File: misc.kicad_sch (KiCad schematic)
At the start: 36 parts

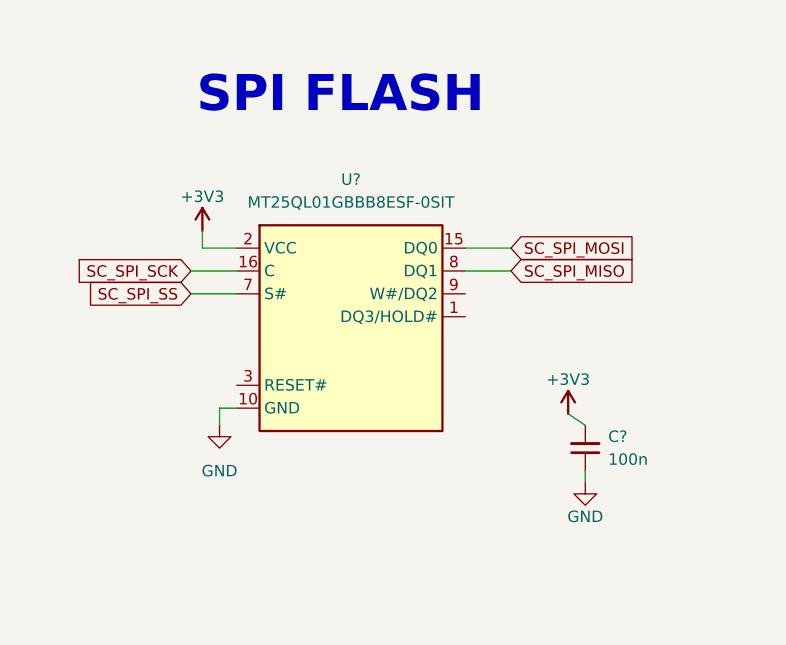
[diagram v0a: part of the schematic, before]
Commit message: [#54272] Change MT25QL01GBBB package
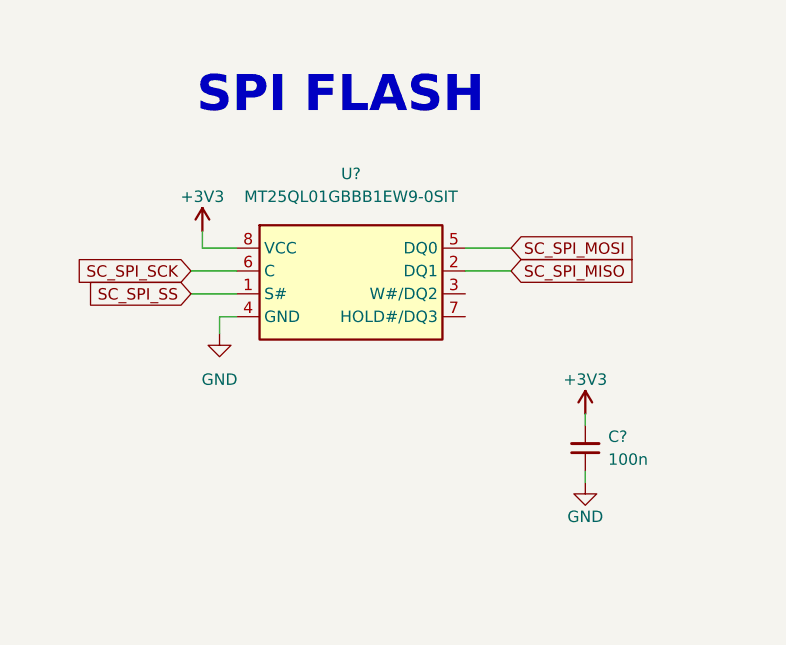
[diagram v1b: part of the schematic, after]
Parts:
- removed U?: MT25QL01GBBB8E_SOP2-16, antmicro-footprints:SOP2-16_7.5x10.3mm, symbol antmicroMemory:MT25QL01GBBB8E_SOP2-16
- added U?: MT25QL01GBBB1EW9-0SIT, antmicro-footprints:W-PDFN-8-1EP_8x6mm_P1.27mm_EP4.3x3.4mm, symbol antmicroMemory:MT25QL01GBBB1EW9-0SIT
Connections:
- net +3V3: now also U?.8 (VCC)
- net GND: now also U?.4 (GND)
- net SC_SPI_MISO: now also U?.2 (DQ1)
- net SC_SPI_MOSI: now also U?.5 (DQ0)
- net SC_SPI_SCK: now also U?.6 (C)
- net SC_SPI_SS: now also U?.1 (S#)
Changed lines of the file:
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@@
     (stroke (width 0) (type default) (color 0 0 0 0))
   )
-  (wire (pts (xy 385.445 204.47) (xy 387.35 205.74))
+  (wire (pts (xy 387.35 204.47) (xy 387.35 205.74))
     (stroke (width 0) (type default) (color 0 0 0 0))
   )
@@
     (stroke (width 0) (type default) (color 0 0 0 0))
   )
-  (wire (pts (xy 348.615 203.835) (xy 346.71 203.835))
+  (wire (pts (xy 348.615 193.675) (xy 346.71 193.675))
     (stroke (width 0) (type default) (color 0 0 0 0))
   )
@@
     (stroke (width 0) (type default) (color 0 0 0 0))
   )
-  (wire (pts (xy 346.71 203.835) (xy 346.71 205.74))
+  (wire (pts (xy 346.71 193.675) (xy 346.71 195.58))
     (stroke (width 0) (type default) (color 0 0 0 0))
   )
@@
     )
   )
-  (symbol (lib_id "antmicropower:+3V3") (at 385.445 204.47 0) (unit 1)
+  (symbol (lib_id "antmicropower:+3V3") (at 387.35 204.47 0) (unit 1)
     (in_bom yes) (on_board yes)
-    (property "Reference" "#PWR?" (id 0) (at 400.685 207.01 0)
+    (property "Reference" "#PWR?" (id 0) (at 402.59 207.01 0)
       (effects (font (size 1.27 1.27) (thickness 0.15)) (justify left bottom) hide)
     )
-    (property "Value" "+3V3" (id 1) (at 385.445 200.66 0)
+    (property "Value" "+3V3" (id 1) (at 387.35 200.66 0)
       (effects (font (size 1.27 1.27) (thickness 0.15)))
     )
-    (property "Footprint" "" (id 2) (at 400.685 212.09 0)
+    (property "Footprint" "" (id 2) (at 402.59 212.09 0)
       (effects (font (size 1.27 1.27) (thickness 0.15)) (justify left bottom) hide)
     )
-    (property "Datasheet" "" (id 3) (at 400.685 214.63 0)
+    (property "Datasheet" "" (id 3) (at 402.59 214.63 0)
       (effects (font (size 1.27 1.27) (thickness 0.15)) (justify left bottom) hide)
     )
-    (property "Author" "Antmicro" (id 4) (at 400.685 212.09 0)
+    (property "Author" "Antmicro" (id 4) (at 402.59 212.09 0)
       (effects (font (size 1.27 1.27) (thickness 0.15)) (justify left bottom) hide)
     )
-    (property "License" "Apache-2.0" (id 5) (at 400.685 214.63 0)
+    (property "License" "Apache-2.0" (id 5) (at 402.59 214.63 0)
       (effects (font (size 1.27 1.27) (thickness 0.15)) (justify left bottom) hide)
     )
@@
     (pin "1")
   )
-  (symbol (lib_id "antmicropower:GND") (at 346.71 205.74 0) (unit 1)
+  (symbol (lib_id "antmicropower:GND") (at 346.71 195.58 0) (unit 1)
     (in_bom yes) (on_board yes) (fields_autoplaced)
-    (property "Reference" "#PWR?" (id 0) (at 355.6 208.28 0)
+    (property "Reference" "#PWR?" (id 0) (at 355.6 198.12 0)
       (effects (font (size 1.27 1.27) (thickness 0.15)) (justify left bottom) hide)
     )
-    (property "Value" "GND" (id 1) (at 346.71 210.82 0)
+    (property "Value" "GND" (id 1) (at 346.71 200.66 0)
       (effects (font (size 1.27 1.27) (thickness 0.15)))
     )
-    (property "Footprint" "" (id 2) (at 355.6 213.36 0)
+    (property "Footprint" "" (id 2) (at 355.6 203.2 0)
       (effects (font (size 1.27 1.27) (thickness 0.15)) (justify left bottom) hide)
     )
-    (property "Datasheet" "" (id 3) (at 355.6 218.44 0)
+    (property "Datasheet" "" (id 3) (at 355.6 208.28 0)
       (effects (font (size 1.27 1.27) (thickness 0.15)) (justify left bottom) hide)
     )
-    (property "Author" "Antmicro" (id 4) (at 355.6 213.36 0)
+    (property "Author" "Antmicro" (id 4) (at 355.6 203.2 0)
       (effects (font (size 1.27 1.27) (thickness 0.15)) (justify left bottom) hide)
     )
-    (property "License" "Apache-2.0" (id 5) (at 355.6 215.9 0)
+    (property "License" "Apache-2.0" (id 5) (at 355.6 205.74 0)
       (effects (font (size 1.27 1.27) (thickness 0.15)) (justify left bottom) hide)
     )
     (pin "1")
   )
-  (symbol (lib_id "antmicroMemory:MT25QL01GBBB8E_SOP2-16") (at 346.075 186.055 0) (unit 1)
-    (in_bom yes) (on_board yes) (fields_autoplaced)
-    (property "Reference" "U?" (id 0) (at 361.315 178.435 0)
-      (effects (font (size 1.27 1.27) (thickness 0.15)))
-    )
-    (property "Value" "MT25QL01GBBB8E_SOP2-16" (id 1) (at 389.255 193.675 0)
-      (effects (font (size 1.27 1.27) (thickness 0.15)) (justify left bottom) hide)
-    )
-    (property "Footprint" "antmicro-footprints:SOP2-16_7.5x10.3mm" (id 2) (at 389.255 196.215 0)
-      (effects (font (size 1.27 1.27) (thickness 0.15)) (justify left bottom) hide)
-    )
-    (property "Datasheet" "https://www.mouser.com/datasheet/2/671/mict_s_a0005338280_1-2290790.pdf" (id 3) (at 389.255 198.755 0)
-      (effects (font (size 1.27 1.27) (thickness 0.15)) (justify left bottom) hide)
-    )
-    (property "MPN" "MT25QL01GBBB8ESF-0SIT" (id 4) (at 361.315 180.975 0)
-      (effects (font (size 1.27 1.27) (thickness 0.15)))
-    )
-    (property "Manufacturer" "Micron Technology" (id 5) (at 389.255 201.295 0)
-      (effects (font (size 1.27 1.27) (thickness 0.15)) (justify left bottom) hide)
-    )
-    (property "VSD_class" "SPI Flash" (id 6) (at 389.255 203.835 0)
-      (effects (font (size 1.27 1.27) (thickness 0.15)) (justify left bottom) hide)
-    )
-    (property "Author" "Antmicro" (id 7) (at 389.255 206.375 0)
-      (effects (font (size 1.27 1.27) (thickness 0.15)) (justify left bottom) hide)
-    )
-    (property "License" "Apache-2.0" (id 8) (at 389.255 208.915 0)
-      (effects (font (size 1.27 1.27) (thickness 0.15)) (justify left bottom) hide)
-    )
-    (pin "1")
-    (pin "10")
-    (pin "11")
-    (pin "12")
-    (pin "13")
-    (pin "14")
-    (pin "15")
-    (pin "16")
-    (pin "2")
-    (pin "3")
-    (pin "4")
-    (pin "5")
-    (pin "6")
-    (pin "7")
-    (pin "8")
-    (pin "9")
-  )
   (symbol (lib_id "antmicroResistors0402:R_49k9_0402") (at 264.16 181.61 90) (unit 1)
     (in_bom yes) (on_board yes)
@@
     (pin "2")
   )
+  (symbol (lib_id "antmicroMemory:MT25QL01GBBB1EW9-0SIT ") (at 348.615 186.055 0) (unit 1)
+    (in_bom yes) (on_board yes) (fields_autoplaced)
+    (property "Reference" "U?" (id 0) (at 361.315 177.8 0)
+      (effects (font (size 1.27 1.27) (thickness 0.15)))
+    )
+    (property "Value" "MT25QL01GBBB1EW9-0SIT " (id 1) (at 391.795 193.675 0)
+      (effects (font (size 1.27 1.27) (thickness 0.15)) (justify left bottom) hide)
+    )
+    (property "Footprint" "antmicro-footprints:W-PDFN-8-1EP_8x6mm_P1.27mm_EP4.3x3.4mm" (id 2) (at 391.795 196.215 0)
+      (effects (font (size 1.27 1.27) (thickness 0.15)) (justify left bottom) hide)
+    )
+    (property "Datasheet" "https://www.mouser.pl/datasheet/2/671/mict_s_a0002234966_1-2290738.pdf" (id 3) (at 391.795 198.755 0)
+      (effects (font (size 1.27 1.27) (thickness 0.15)) (justify left bottom) hide)
+    )
+    (property "MPN" "MT25QL01GBBB1EW9-0SIT " (id 4) (at 361.315 180.34 0)
+      (effects (font (size 1.27 1.27) (thickness 0.15)))
+    )
+    (property "Manufacturer" "Micron Technology" (id 5) (at 391.795 201.295 0)
+      (effects (font (size 1.27 1.27) (thickness 0.15)) (justify left bottom) hide)
+    )
+    (property "VSD_class" "SPI Flash" (id 6) (at 391.795 203.835 0)
+      (effects (font (size 1.27 1.27) (thickness 0.15)) (justify left bottom) hide)
+    )
+    (property "Author" "Antmicro" (id 7) (at 391.795 206.375 0)
+      (effects (font (size 1.27 1.27) (thickness 0.15)) (justify left bottom) hide)
+    )
+    (property "License" "Apache-2.0" (id 8) (at 391.795 208.915 0)
+      (effects (font (size 1.27 1.27) (thickness 0.15)) (justify left bottom) hide)
+    )
+    (pin "1")
+    (pin "2")
+    (pin "3")
+    (pin "4")
+    (pin "5")
+    (pin "6")
+    (pin "7")
+    (pin "8")
+  )
   (symbol (lib_id "antmicroResistors0402:R_49k9_0402") (at 261.62 181.61 90) (unit 1)

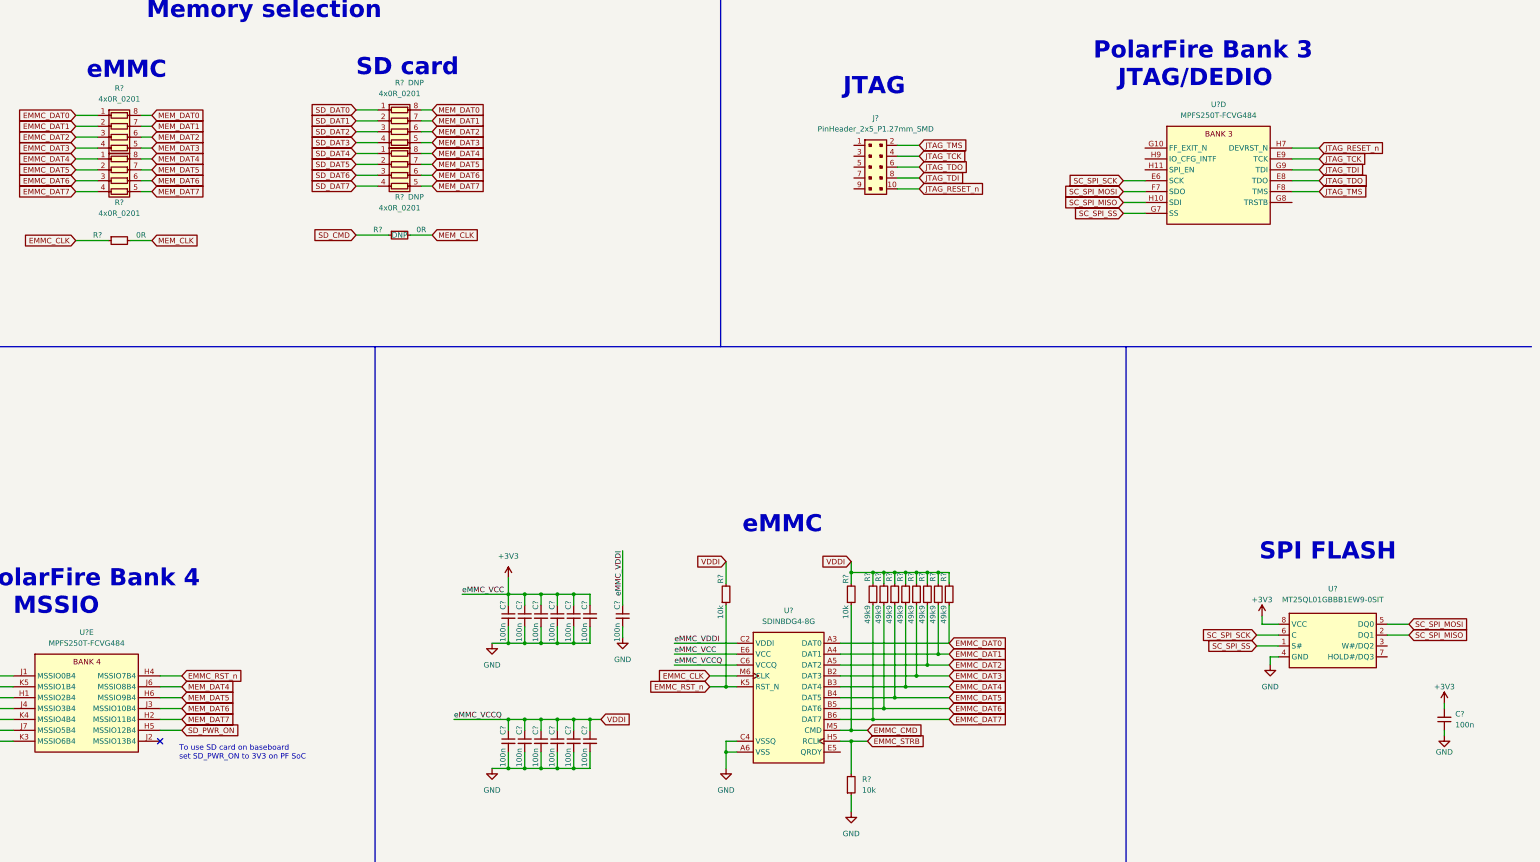
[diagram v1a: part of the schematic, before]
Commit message: [#54016] Place components to assess available space
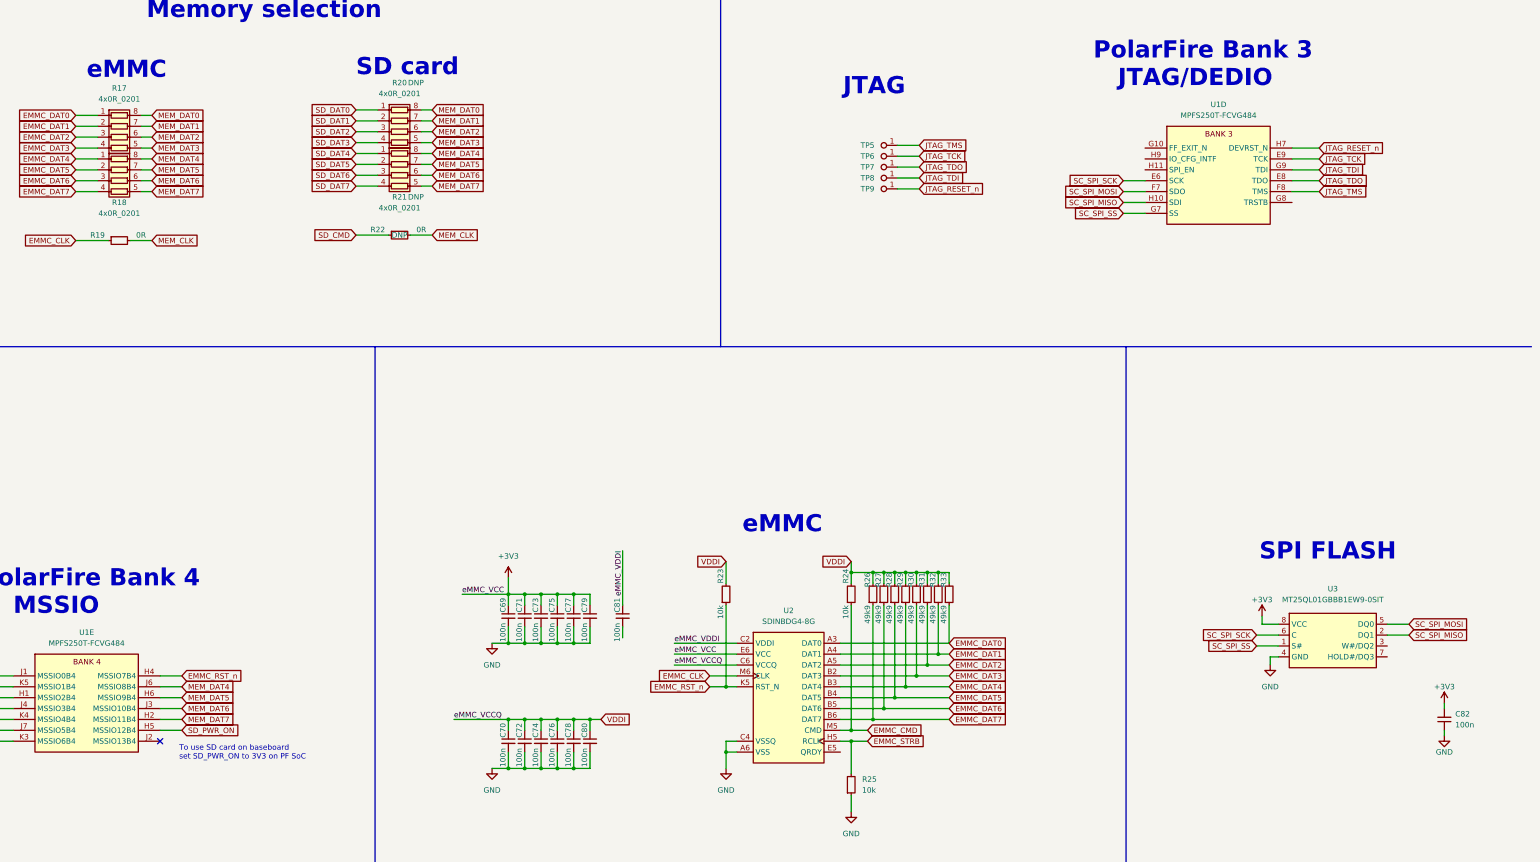
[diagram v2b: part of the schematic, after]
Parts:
- removed J?: PinHeader_2x5_P1.27mm_SMD, antmicro-footprints:PinHeader_2x5_P1.27mm_SMD, symbol antmicroGenericPinHeaders:PinHeader_2x5_P1.27mm_SMD
- removed U?: MT25QL01GBBB1EW9-0SIT, antmicro-footprints:W-PDFN-8-1EP_8x6mm_P1.27mm_EP4.3x3.4mm, symbol antmicroMemory:MT25QL01GBBB1EW9-0SIT
- added TP5, TP6, TP7, TP8, TP9: TP_0.75mm_SMD, antmicro-footprints:TP_SMD_0.75mm, symbol antmicroTestPoints:TP_0.75mm_SMD
- added U3: MT25QL01GBBB1EW9-0SIT, antmicro-footprints:W-PDFN-8-1EP_8x6mm_P1.27mm_EP4.3x3.4mm, symbol antmicroMemory:MT25QL01GBBB1EW9-0SIT
- gave numbers to parts that had none: 33
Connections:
- net +3V3: now also U3.8 (VCC)
- net GND: now also U3.4 (GND); no longer C81.2
- net JTAG_RESET_n: now also TP9.1
- net JTAG_TCK: now also TP6.1
- net JTAG_TDI: now also TP8.1
- net JTAG_TDO: now also TP7.1
- net JTAG_TMS: now also TP5.1
- net SC_SPI_MISO: now also U3.2 (DQ1)
- net SC_SPI_MOSI: now also U3.5 (DQ0)
- net SC_SPI_SCK: now also U3.6 (C)
- net SC_SPI_SS: now also U3.1 (S#)

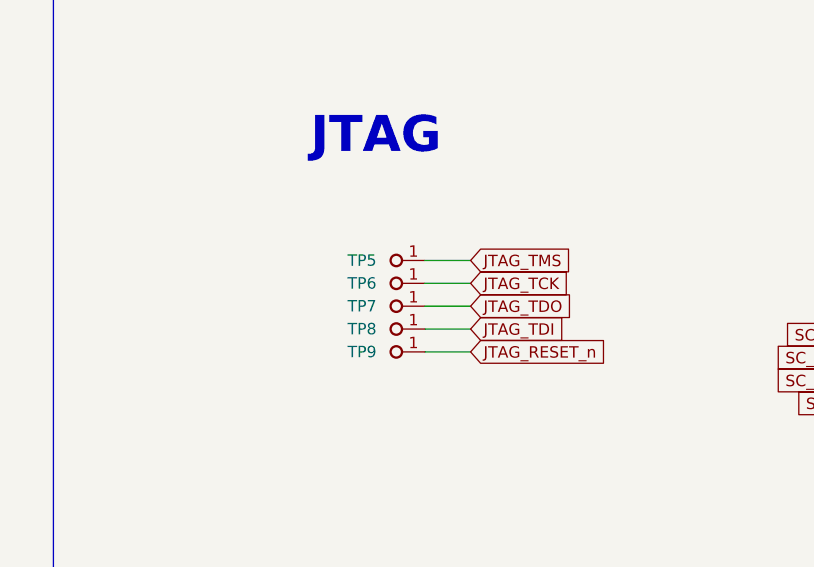
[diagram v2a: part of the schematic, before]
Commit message: [#54178] Add Tag-Connect
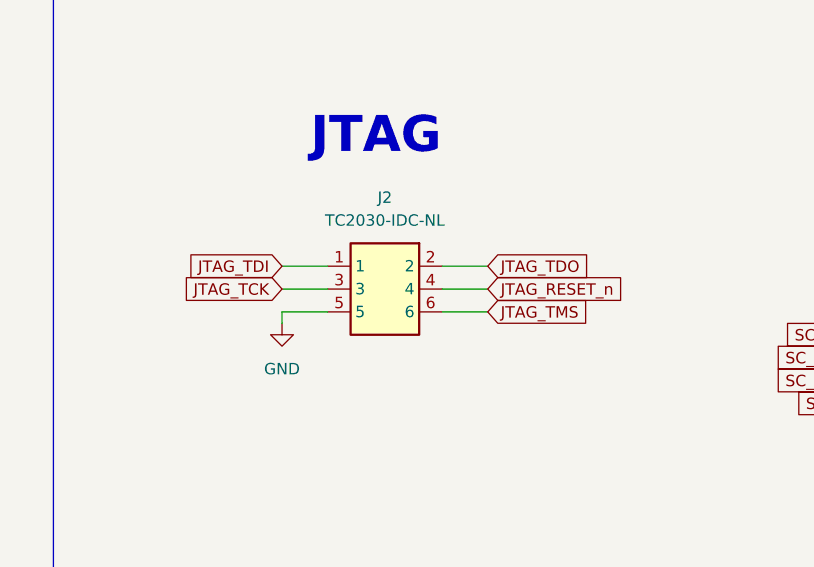
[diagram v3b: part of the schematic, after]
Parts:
- removed TP5, TP6, TP7, TP8, TP9: TP_0.75mm_SMD, antmicro-footprints:TP_SMD_0.75mm, symbol antmicroTestPoints:TP_0.75mm_SMD
- added J2: Tag-Connect_TC2030-IDC-NL_2x3_P1.27mm, antmicro-footprints:Tag-Connect_TC2030-IDC-NL_2x3_P1.27mm, symbol antmicroTestPoints:Tag-Connect_TC2030-IDC-NL_2x3_P1.27mm
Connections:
- net GND: now also J2.5
- net JTAG_RESET_n: now also J2.4
- net JTAG_TCK: now also J2.3
- net JTAG_TDI: now also J2.1
- net JTAG_TDO: now also J2.2
- net JTAG_TMS: now also J2.6

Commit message: [#54491] Minor adjustments of labels and graphical items
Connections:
- net GND: now also C81.2
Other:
- moved on the sheet: R17, R18, R19, R21, R22, R24, R26, R27, R28, R29, R30, R31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
